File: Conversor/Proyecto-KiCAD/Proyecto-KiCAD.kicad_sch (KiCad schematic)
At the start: 48 parts, among them Q1 IRFP150, Q2 IRFP150, Q3 IRFP150, Q4 IRFP150

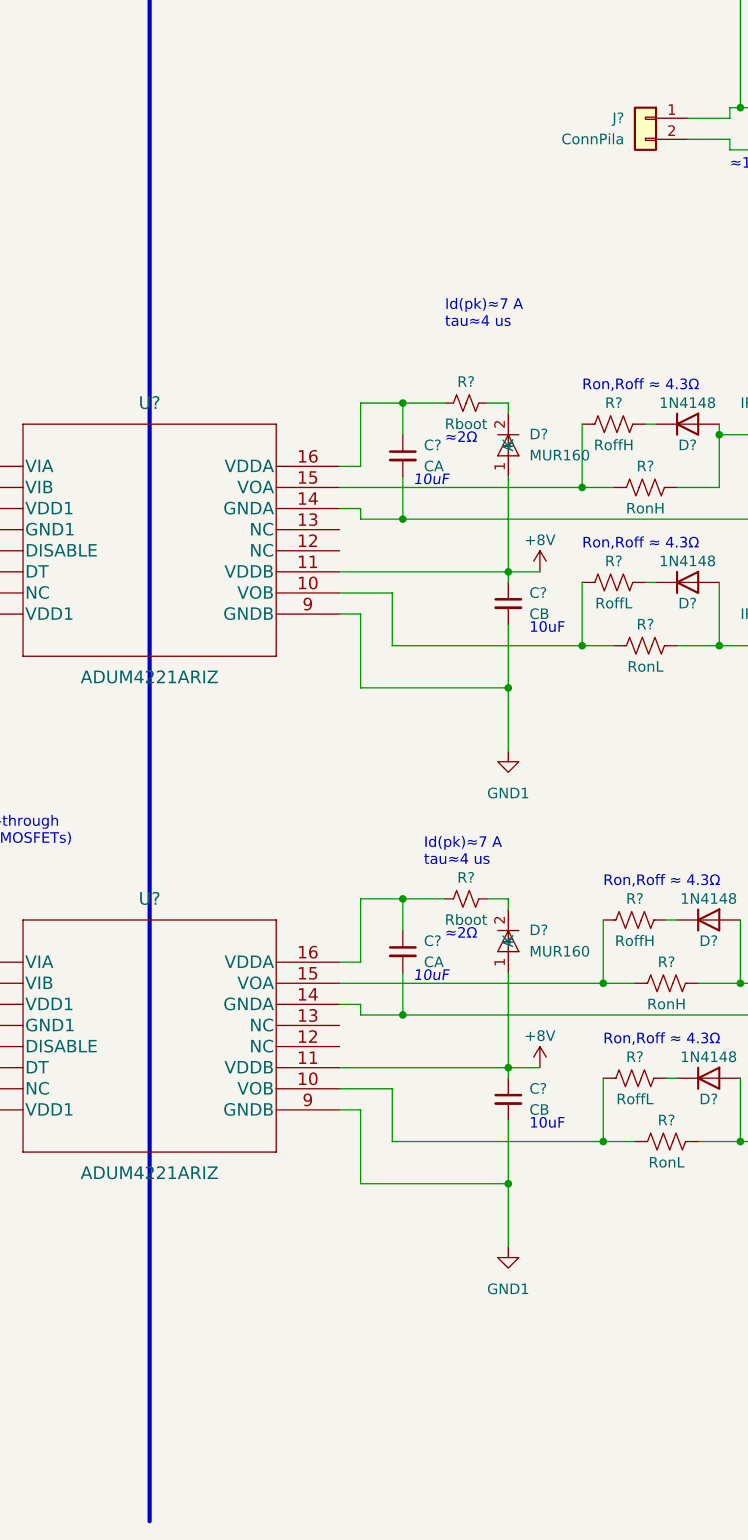
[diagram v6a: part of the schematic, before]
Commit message: Seleccion definitiva de drivers y sensores (ya comprados)
- Driver Infineon 2ED21834-S06J: Con DT y sin asilamiento
  - Optoacopladores ACPL-P480 para aislarlos
  - Falta implementarlos (drivers y optos) en el esquematico
- LM5056 como sensor de corriente de entrada y tension de entrada/salida
- Sensor de efecto hall TMCS1100A4 para corriente de salida
  - Ya esta agregado al esquematico (reemplazo ACS709)
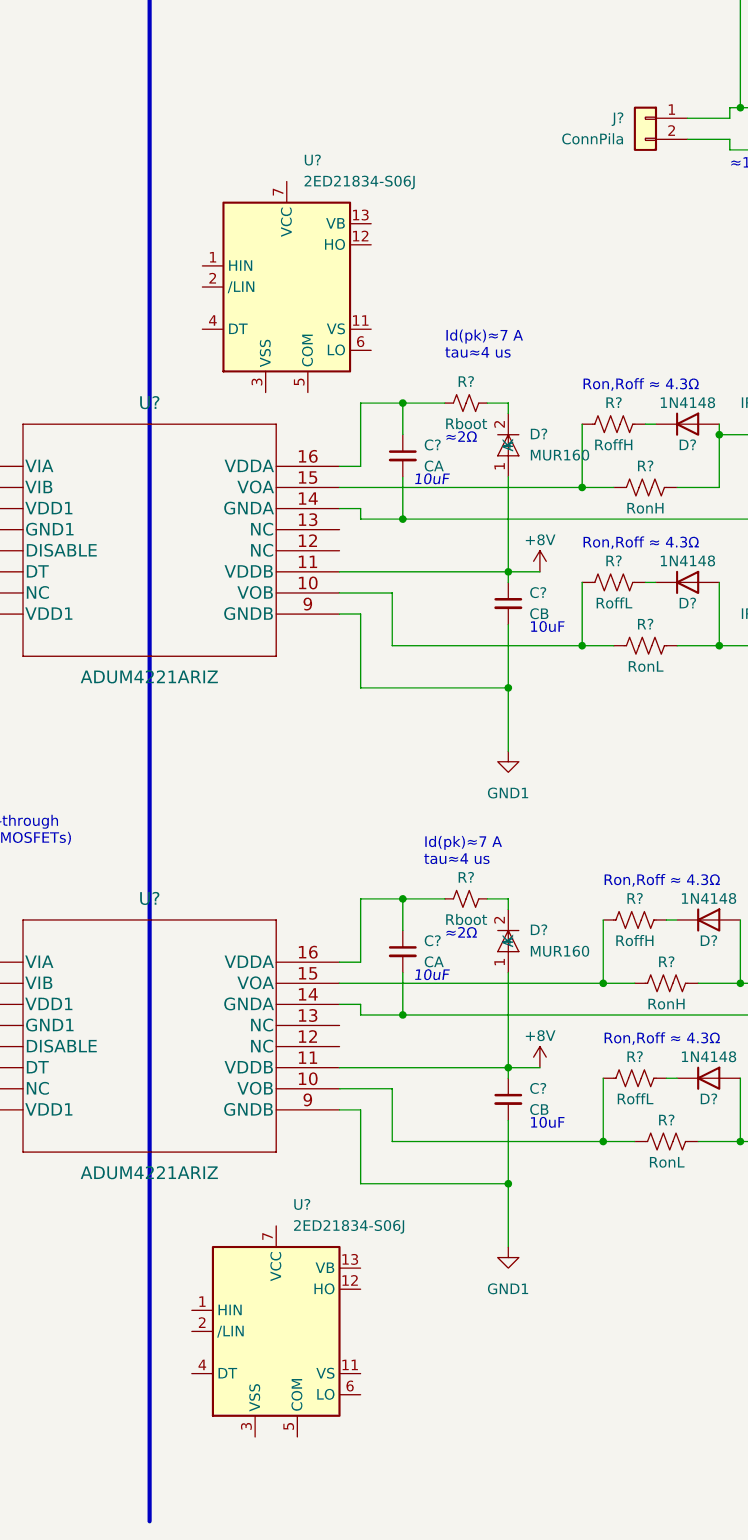
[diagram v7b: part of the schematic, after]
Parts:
- added U? (x2): 2ED21834-S06J, Package_SO:SOIC-14_3.9x8.7mm_P1.27mm, symbol Componentes proyecto:2ED21834-S06J
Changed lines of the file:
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@@
     (stroke (width 0) (type default) (color 0 0 0 0))
   )
-  (text "Id(pk)≈7 A\ntau≈4 us" (at 132.08 129.54 0)
+  (text "Id(pk)≈7 A\ntau≈4 us" (at 132.08 133.35 0)
     (effects (font (size 1.27 1.27)) (justify left bottom))
   )
@@
     (pin "2")
   )
+  (symbol (lib_id "Componentes proyecto:2ED21834-S06J") (at 113.03 124.46 0) (unit 1)
+    (in_bom yes) (on_board yes) (fields_autoplaced)
+    (property "Reference" "U?" (id 0) (at 115.0494 109.22 0)
+      (effects (font (size 1.27 1.27)) (justify left))
+    )
+    (property "Value" "2ED21834-S06J" (id 1) (at 115.0494 111.76 0)
+      (effects (font (size 1.27 1.27)) (justify left))
+    )
+    (property "Footprint" "Package_SO:SOIC-14_3.9x8.7mm_P1.27mm" (id 2) (at 113.03 124.46 0)
+      (effects (font (size 1.27 1.27)) hide)
+    )
+    (property "Datasheet" "" (id 3) (at 113.03 124.46 0)
+      (effects (font (size 1.27 1.27)) hide)
+    )
+    (pin "1")
+    (pin "10")
+    (pin "11")
+    (pin "12")
+    (pin "13")
+    (pin "14")
+    (pin "2")
+    (pin "3")
+    (pin "4")
+    (pin "5")
+    (pin "6")
+    (pin "7")
+    (pin "8")
+    (pin "9")
+  )
   (symbol (lib_id "power:GNDD") (at 69.85 236.22 0) (unit 1)
     (in_bom yes) (on_board yes) (fields_autoplaced)
@@
     )
     (pin "1")
+  )
+  (symbol (lib_id "Componentes proyecto:2ED21834-S06J") (at 111.76 250.19 0) (unit 1)
+    (in_bom yes) (on_board yes) (fields_autoplaced)
+    (property "Reference" "U?" (id 0) (at 113.7794 234.95 0)
+      (effects (font (size 1.27 1.27)) (justify left))
+    )
+    (property "Value" "2ED21834-S06J" (id 1) (at 113.7794 237.49 0)
+      (effects (font (size 1.27 1.27)) (justify left))
+    )
+    (property "Footprint" "Package_SO:SOIC-14_3.9x8.7mm_P1.27mm" (id 2) (at 111.76 250.19 0)
+      (effects (font (size 1.27 1.27)) hide)
+    )
+    (property "Datasheet" "" (id 3) (at 111.76 250.19 0)
+      (effects (font (size 1.27 1.27)) hide)
+    )
+    (pin "1")
+    (pin "10")
+    (pin "11")
+    (pin "12")
+    (pin "13")
+    (pin "14")
+    (pin "2")
+    (pin "3")
+    (pin "4")
+    (pin "5")
+    (pin "6")
+    (pin "7")
+    (pin "8")
+    (pin "9")
   )
   (symbol (lib_id "Connector_Generic:Conn_01x02") (at 251.46 152.4 0) (unit 1)
@@
       (reference "#PWR?") (unit 1) (value "GNDD") (footprint "")
     )
-    (path "/02b36b52-6a67-4b1a-aeda-ca74c124cf8d/8f596512-7697-4c9a-b893-7ea997d561ce"
-      (reference "#PWR?") (unit 1) (value "GNDD") (footprint "")
-    )
     (path "/a09a2ace-9aae-478b-9899-37e247701037"
       (reference "#PWR?") (unit 1) (value "+8V") (footprint "")
@@
       (reference "#PWR?") (unit 1) (value "GNDD") (footprint "")
     )
-    (path "/02b36b52-6a67-4b1a-aeda-ca74c124cf8d/e58b7a0f-4d12-4812-ae2f-4e3648a81a80"
-      (reference "#PWR?") (unit 1) (value "GNDD") (footprint "")
-    )
     (path "/e7a7275a-867c-487d-979b-bed76ac18aff"
       (reference "#PWR?") (unit 1) (value "GND1") (footprint "")
@@
       (reference "C?") (unit 1) (value "CREG_OUT") (footprint "")
     )
-    (path "/02b36b52-6a67-4b1a-aeda-ca74c124cf8d/415c5832-2e48-42c0-be91-9af1e8558e9f"
-      (reference "C?") (unit 1) (value "CF") (footprint "")
-    )
     (path "/02b36b52-6a67-4b1a-aeda-ca74c124cf8d/46224676-57df-4b0a-bf24-46723abd2afa"
       (reference "C?") (unit 1) (value "C") (footprint "")
@@
       (reference "C?") (unit 1) (value "Cvdd") (footprint "")
     )
-    (path "/02b36b52-6a67-4b1a-aeda-ca74c124cf8d/f83eefe3-b23a-4373-89c1-2b12ef6b97bb"
-      (reference "C?") (unit 1) (value "Cvzcr") (footprint "")
-    )
     (path "/c7cb9e9c-966f-4c42-adfd-0815e2342bf1"
       (reference "D1") (unit 1) (value "MUR860") (footprint "Package_TO_SOT_THT:TO-220F-2_Vertical")
@@
       (reference "J?") (unit 1) (value "ConnPWM1324") (footprint "")
     )
-    (path "/02b36b52-6a67-4b1a-aeda-ca74c124cf8d/c0496552-7acb-4688-af06-d355ca35898d"
-      (reference "J?") (unit 1) (value "ConnOC") (footprint "")
-    )
     (path "/f2aa065b-e896-4b6a-ab8f-8acc1fb2caeb"
       (reference "J?") (unit 1) (value "ConnTrafoP") (footprint "")
@@
       (reference "R?") (unit 1) (value "Rpu") (footprint "")
     )
+    (path "/02b36b52-6a67-4b1a-aeda-ca74c124cf8d/2eb1d93a-db41-4c8c-bc48-983860bd693d"
+      (reference "U?") (unit 1) (value "TMCS1100A4") (footprint "")
+    )
     (path "/02b36b52-6a67-4b1a-aeda-ca74c124cf8d/47b8ea16-dc3e-4c48-bfd5-4c7615e3b200"
       (reference "U?") (unit 1) (value "ISO7242C") (footprint "")
@@
       (reference "U?") (unit 1) (value "LM5056APMH/NOPB") (footprint "PWP28_TEX")
     )
-    (path "/02b36b52-6a67-4b1a-aeda-ca74c124cf8d/65195532-8b87-43dc-9b66-e82bde4fa215"
-      (reference "U?") (unit 1) (value "ACS709") (footprint "Package_SO:SSOP-24_3.9x8.7mm_P0.635mm")
-    )
     (path "/66a2fb96-f7f8-481c-8036-16047d50af8a"
       (reference "U?") (unit 1) (value "ADUM4221ARIZ") (footprint "RI-16-2_Creepage_ADI")
@@
       (reference "U?") (unit 1) (value "MC7805") (footprint "")
     )
+    (path "/b668cbbc-478a-4099-92a3-24a206c3a9b9"
+      (reference "U?") (unit 1) (value "2ED21834-S06J") (footprint "Package_SO:SOIC-14_3.9x8.7mm_P1.27mm")
+    )
     (path "/59d8992c-71f3-4d96-a665-43f8d7d91dab/e573024c-7f98-4b31-a0c9-502cb18bd081"
       (reference "U?") (unit 1) (value "LM1117-3.3") (footprint "")
     )
-  )
+    (path "/f2a09b35-24d8-43c7-adfb-783f44046977"
+      (reference "U?") (unit 1) (value "2ED21834-S06J") (footprint "Package_SO:SOIC-14_3.9x8.7mm_P1.27mm")
+    )
+  )

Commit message: Reemplazar drivers aislados por driver+optos
- Solo faltaria ver la alimentacion de +15V para los dos drivers
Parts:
- removed C? (x2): Cvcci, symbol Device:C_Small
- removed C? (x2): CB, symbol Device:C_Small
- removed C? (x2): CA, symbol Device:C_Small
- removed D? (x2): MUR160, symbol Componentes proyecto:MUR160
- removed D? (x4): 1N4148, Diode_THT:D_DO-35_SOD27_P7.62mm_Horizontal, symbol Diode:1N4148
- removed R? (x2): RoffL, symbol Device:R_US
- removed R? (x2): RonH, symbol Device:R_US
- removed R? (x2): RoffH, symbol Device:R_US
- removed R? (x2): Rboot, symbol Device:R_Small_US
- removed R? (x2): RDT, symbol Device:R_Small_US
- removed R? (x2): RonL, symbol Device:R_US
- removed U? (x2): ADUM4221ARIZ, RI-16-2_Creepage_ADI, symbol 2022-05-17_16-55-27:ADUM4221ARIZ
- added C? (x2): Cboot, symbol Device:C_Small
- added C? (x4): C, symbol Device:C_Small
- added C? (x2): CDT, symbol Device:C_Small
- added C? (x2): CVCC, symbol Device:C_Small
- added R? (x2): RonL, symbol Device:R_US
- added R? (x2): RonH, symbol Device:R_US
- added R? (x2): RS, symbol Device:R_US
- added U? (x4): ACPL-P480, Package_SO:SSO-6_6.8x4.6mm_P1.27mm_Clearance7mm, symbol Componentes proyecto:ACPL-P480
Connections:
- net GND1: now also U?.3 (VSS), U?.3 (VSS), U?.5 (COM), U?.5 (COM), C?.1, C?.1, C?.2, C?.2, C?.2, C?.2, C?.2, C?.2, U?.4 (VO), U?.4 (VO), U?.4 (VO), U?.4 (VO)
- net GNDD: now also U?.3 (K), U?.3 (K), U?.3 (K), U?.3 (K)
- net at Q1.2 (G): now also R?.2
- net VS2-4: now reaches C2.2, C4.1, J?.2 (Pin_2), Q2.3 (S), Q4.1 (D)
- net VS2-4: now also R?.2
- net at Q3.2 (G): now also R?.2
- net at C1.2, C3.1, J?.1 (Pin_1)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: now also R?.2
- net at J?.3 (Pin_3): now also U?.1 (A)
- net at J?.4 (Pin_4): now also U?.1 (A)
- net at J?.1 (Pin_1): now also U?.1 (A)
- net at J?.2 (Pin_2): now also U?.1 (A)
- net VG2: now reaches Q2.2 (G)
- net VG2: now also R?.2
- net at U?.1 (HIN): now also U?.4 (VO) (x2)
- net at U?.11 (VS): now also C?.2, R?.1 (x2)
- net at U?.12 (HO): now also R?.1 (x2)
- net at U?.13 (VB): now also C?.1 (x2)
- net at U?.2 (/LIN): now also U?.4 (VO) (x2)
- net at U?.4 (DT): now also C?.1 (x2)
- net at U?.6 (LO): now also R?.1 (x2)
- net +15V: now reaches U?.7 (VCC)
- net +15V: now also U?.7 (VCC), C?.2, C?.2
- net VG4: now reaches Q4.2 (G)
- net VG4: now also R?.2
- new net +5VP: C?.1, C?.1, C?.1, C?.1, U?.6 (VCC), U?.6 (VCC), U?.6 (VCC), U?.6 (VCC)
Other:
- note added: "100nF"
- note added: "10nF"
- note added: "1uF"
- note added: "200nF"
- note added: "2Ω"
- note added: "5Ω"
- note added: "RS para reducir picos negativos de VS"
- note added: "tDT=400ns @ RDT=0Ω"
- note removed: "0.1uF"
- note removed: "10uF"
- note removed: "20kΩ"
- note removed: "Id(pk)≈7 A tau≈4 us"
- note removed: "Ron,Roff ≈ 4.3Ω"
- note removed: "tDT[ns]=5*RDT[kΩ]=100ns"
- note removed: "≈2Ω"
- moved on the sheet: C1, C2, C3, C4, C?, D1, D2, D3, D4, J?, Q1, Q2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
